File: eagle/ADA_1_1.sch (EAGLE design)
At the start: 14 parts, among them X1 A, X10 B, X2 A, X3 A, X4 A, X5 B, X6 B, X7 B, X8 B, X9 A

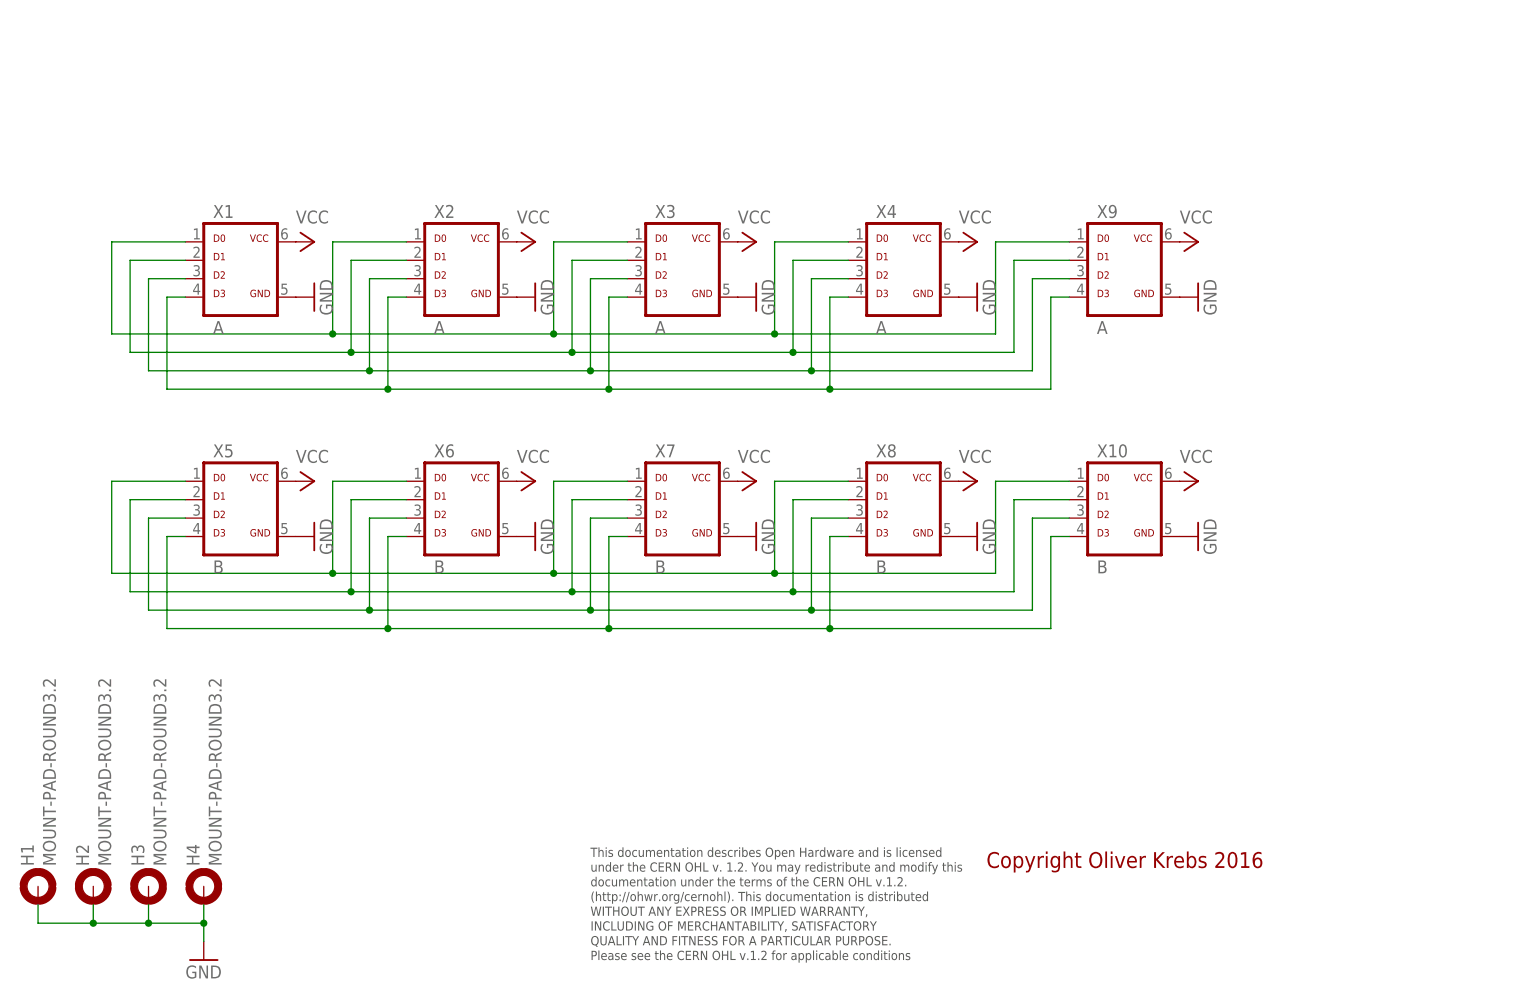
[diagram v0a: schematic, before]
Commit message: Add new tetra-Board and arduino files
Add AMP_1_0, AVC_1_0, D18_1_1, IOP_1_2, MIC_1_0, PIN_1_1, POT_1_0, PWA_1_0, PWR_1_0, RGF 2.0, SOC_2_0, VLT_1_0
Add mex_nano_shield_keyboard, mex_nano_shied_numbers

New arduino projects
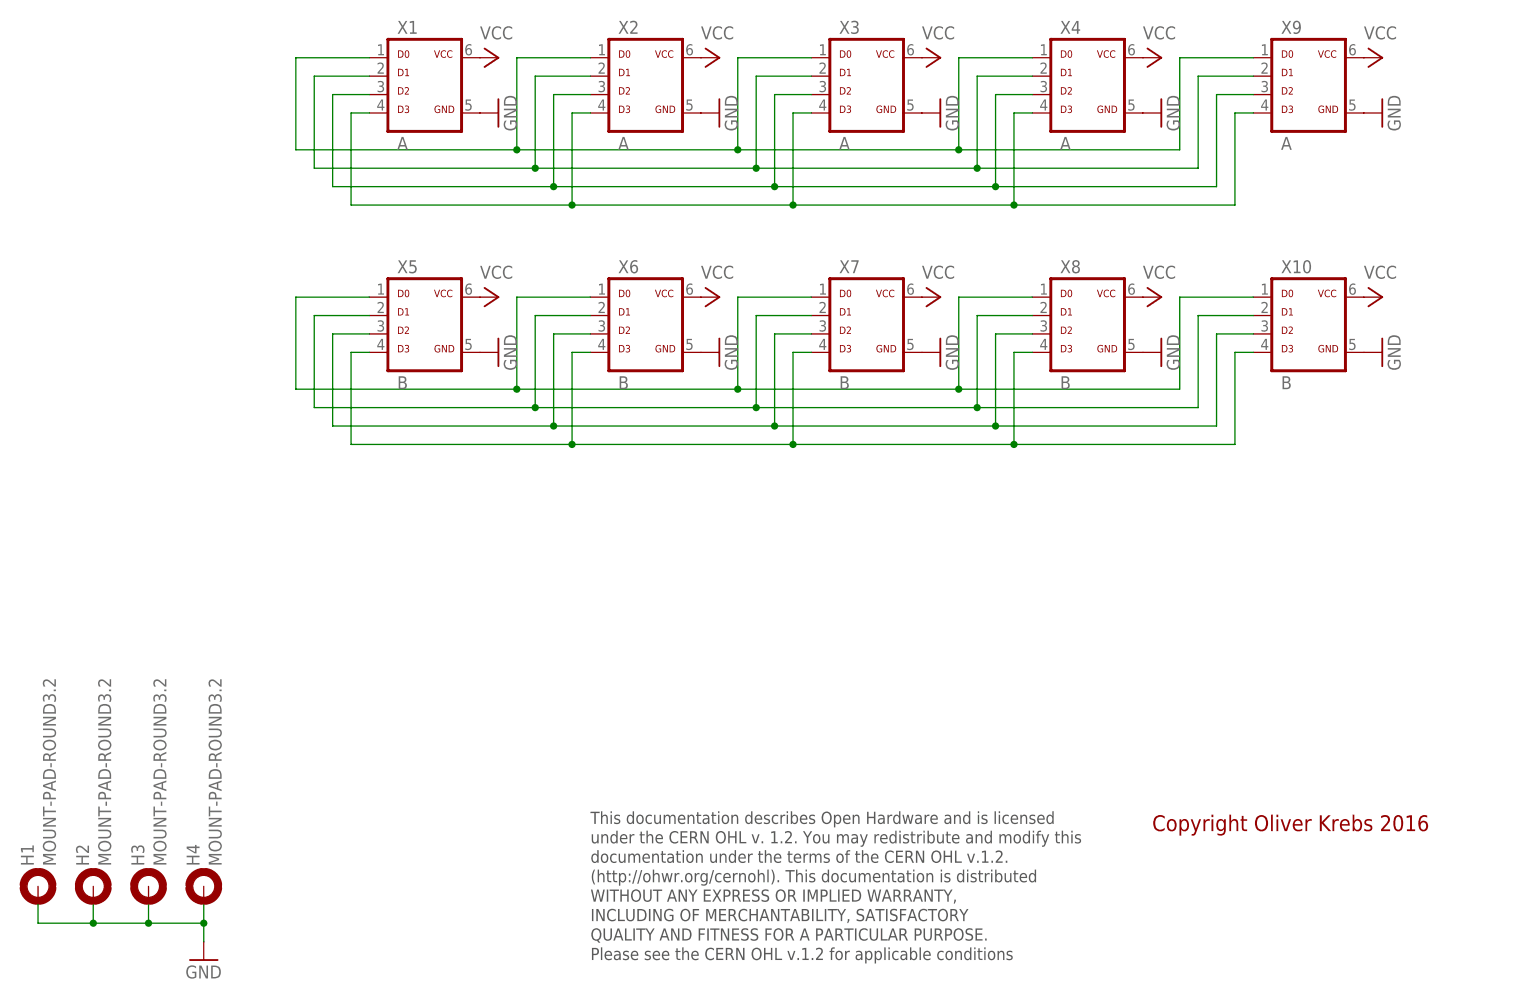
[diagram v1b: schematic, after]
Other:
- moved on the sheet: X1, X10, X2, X3, X4, X5, X6, X7, X8, X9
